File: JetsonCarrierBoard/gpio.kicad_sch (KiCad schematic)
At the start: 19 parts

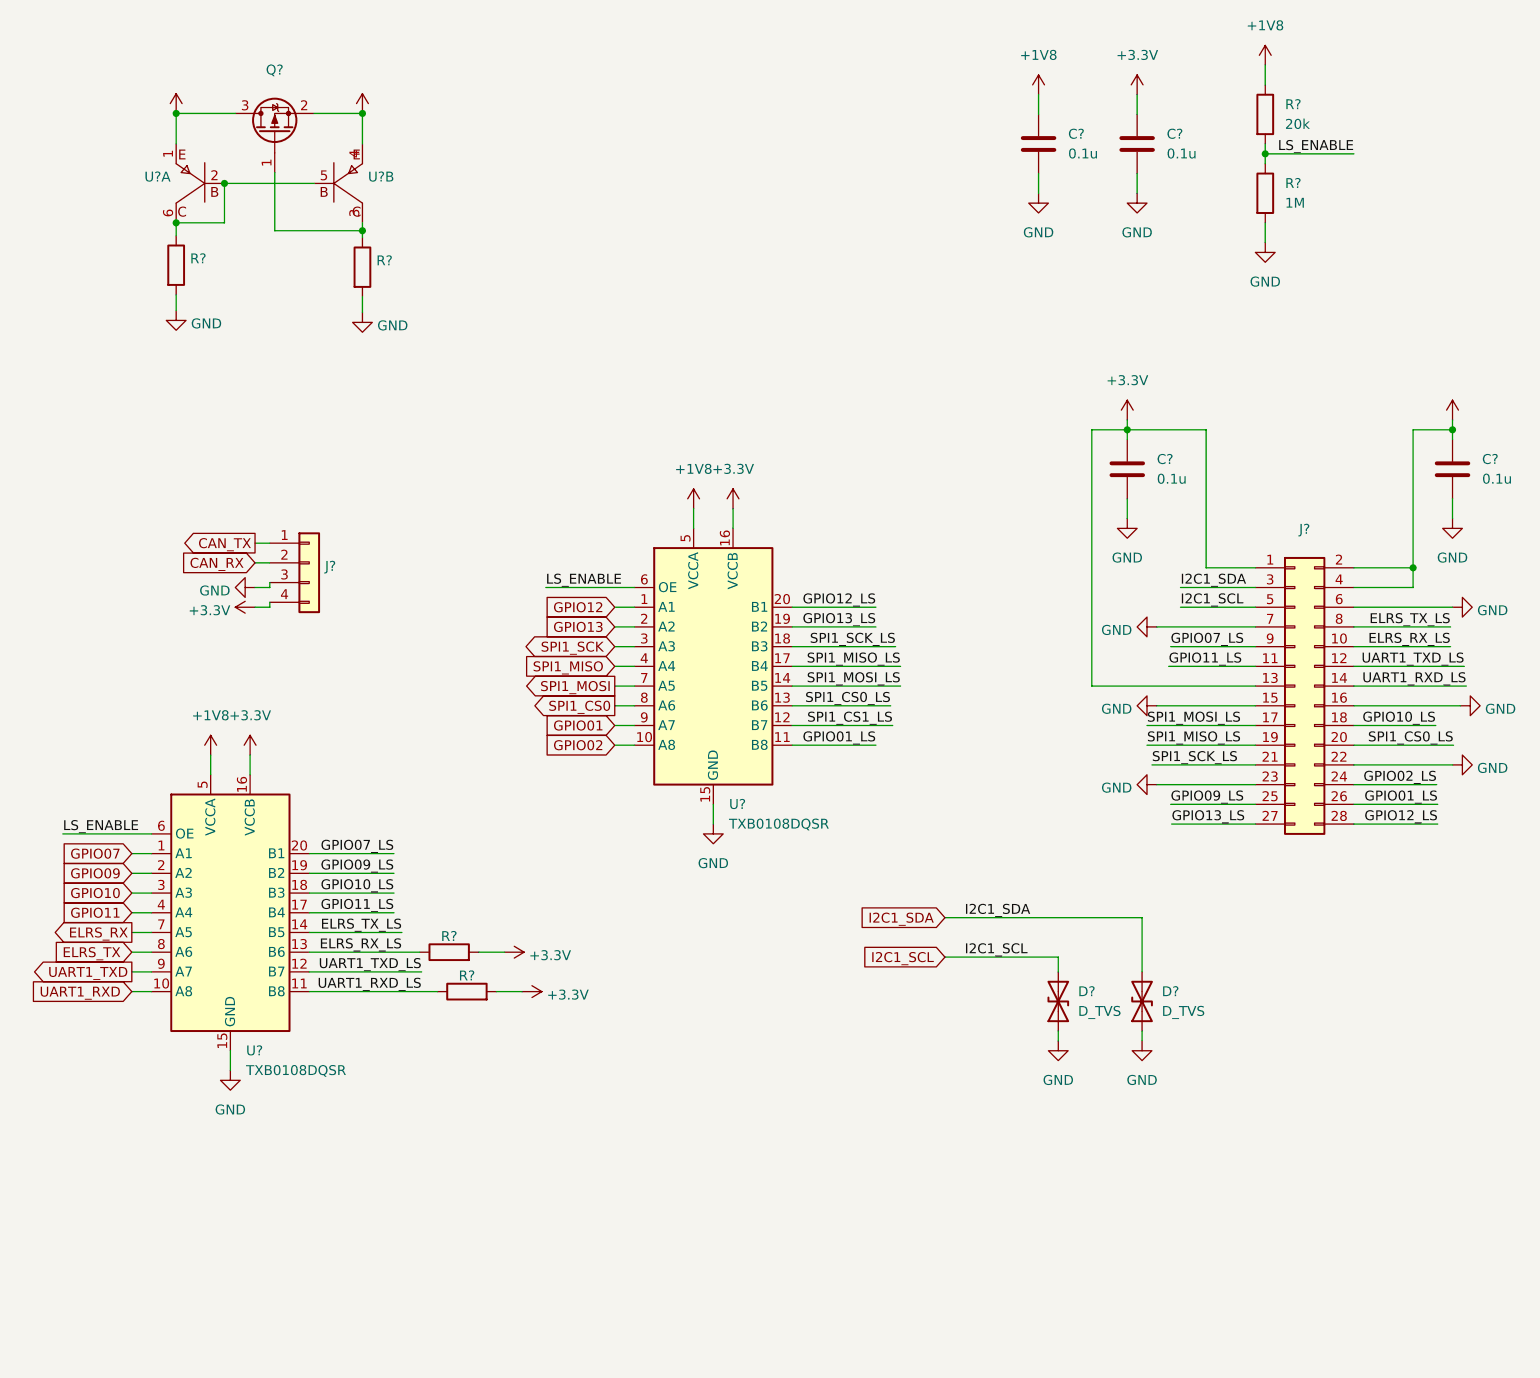
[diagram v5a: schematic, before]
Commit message: Improvement list, fixes, and readability improvements
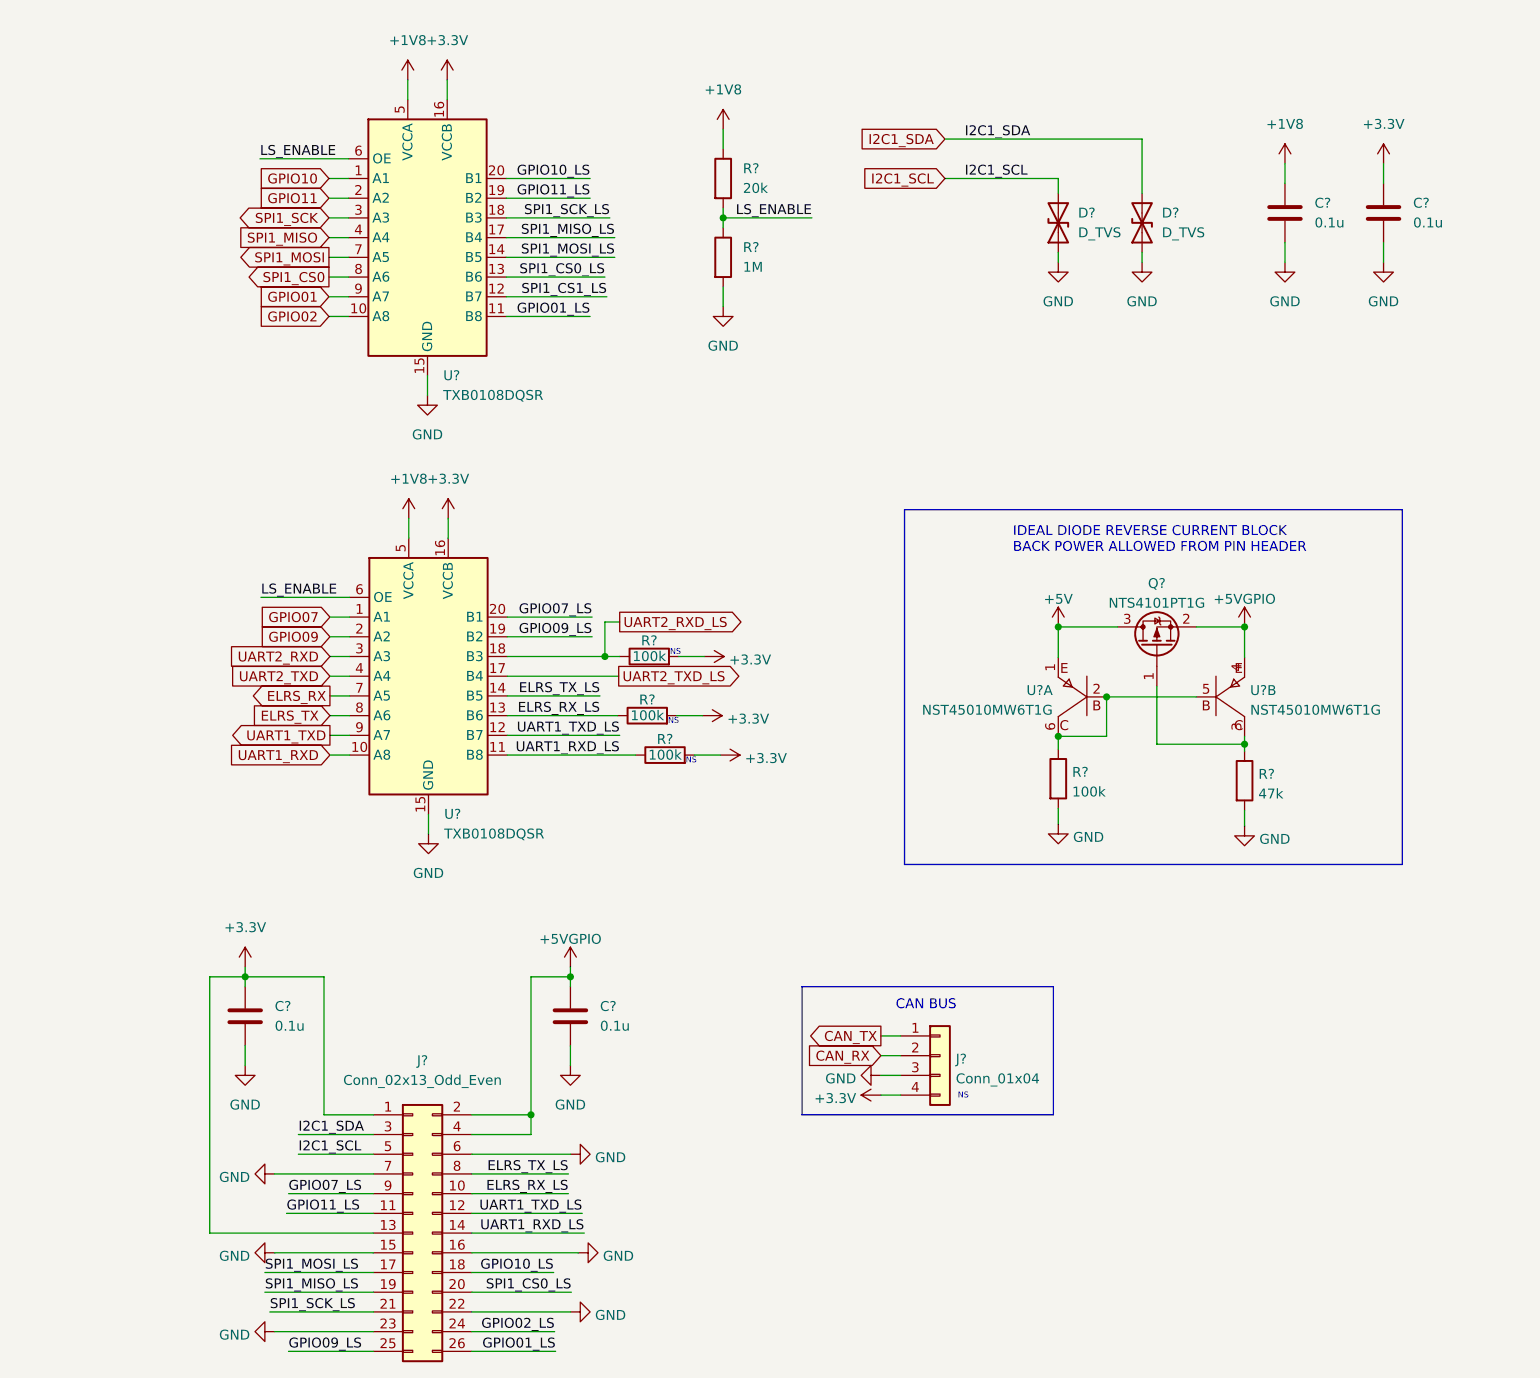
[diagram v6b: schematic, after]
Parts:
- removed J?: (no value), symbol Connector_Generic:Conn_02x14_Odd_Even
- added J?: Conn_02x13_Odd_Even, symbol Connector_Generic:Conn_02x13_Odd_Even
- added R?: 100k, symbol Device:R
- J?: value (none) -> Conn_01x04
- Q?: value (none) -> NTS4101PT1G; footprint (none) -> Package_TO_SOT_SMD:SOT-23
- R? (x3): value (none) -> 100k
- R?: value (none) -> 47k
- U? (x2): value (none) -> NST45010MW6T1G
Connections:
- net GPIO12 is gone; now on net GPIO10: U?.1 (A1)
- net GPIO12_LS is gone; now on net GPIO10_LS: U?.20 (B1)
- net GPIO13 is gone; now on net GPIO11: U?.2 (A2)
- net GPIO13_LS is gone; now on net GPIO11_LS: U?.19 (B2)
- net +20V: now also J?.2 (Pin_2), J?.4 (Pin_4)
- net +3.3V: now also J?.1 (Pin_1), J?.13 (Pin_13), R?.2
- net ELRS_RX_LS: now also J?.10 (Pin_10)
- net ELRS_TX_LS: now also J?.8 (Pin_8)
- net GND: now also J?.15 (Pin_15), J?.16 (Pin_16), J?.22 (Pin_22), J?.23 (Pin_23), J?.6 (Pin_6), J?.7 (Pin_7)
- net GPIO01_LS: now also J?.26 (Pin_26)
- net GPIO02_LS: now also J?.24 (Pin_24)
- net GPIO07_LS: now also J?.9 (Pin_9)
- net GPIO09_LS: now also J?.25 (Pin_25)
- net GPIO10: no longer U?.3 (A3)
- net GPIO10_LS: now also J?.18 (Pin_18); no longer U?.18 (B3)
- net GPIO11: no longer U?.4 (A4)
- net GPIO11_LS: now also J?.11 (Pin_11); no longer U?.17 (B4)
- net I2C1_SCL: now also J?.5 (Pin_5)
- net I2C1_SDA: now also J?.3 (Pin_3)
- net SPI1_CS0_LS: now also J?.20 (Pin_20)
- net SPI1_MISO_LS: now also J?.19 (Pin_19)
- net SPI1_MOSI_LS: now also J?.17 (Pin_17)
- net SPI1_SCK_LS: now also J?.21 (Pin_21)
- net UART1_RXD_LS: now also J?.14 (Pin_14)
- net UART1_TXD_LS: now also J?.12 (Pin_12)
- new net UART2_RXD: U?.3 (A3)
- new net UART2_RXD_LS: R?.1, U?.18 (B3)
- new net UART2_TXD: U?.4 (A4)
- new net UART2_TXD_LS: U?.17 (B4)
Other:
- note added: "CAN BUS"
- note added: "IDEAL DIODE REVERSE CURRENT BLOCK BACK POWER ALLOWED FROM PIN HEADER"
- note added: "NS"
- moved on the sheet: C?, D?, J?, Q?, R?, U?, U?A, U?B
